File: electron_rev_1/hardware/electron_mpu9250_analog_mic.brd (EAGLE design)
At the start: 22.2 x 102.8 mm, 43 parts, among them IC2 S25FL128SAGNFI011, IC4 MIC_I2S_SPH0645, U1 MPU-9250, U10 GAS_SENSOR, U2 Value, U3 OPA322AIDBVT, U4 microSD, U5 +12v, U6 +12v, U7 GAS_SENSOR

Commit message: mainly cosmetic changes to schematic. changed label types
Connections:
- removed net AUX_CL: U1.7
- removed net AUX_DA: U1.21
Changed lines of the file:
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@@
 <contactref element="U7" pad="HB"/>
 <contactref element="U10" pad="HB"/>
-<contactref element="U4" pad="CD2"/>
 <contactref element="U4" pad="6"/>
 <contactref element="U4" pad="GND1"/>
@@
 <via x="18.81" y="-6.02" extent="1-16" drill="0.2"/>
 <via x="5.36" y="13.64" extent="1-16" drill="0.2"/>
+<contactref element="U4" pad="CD2"/>
 </signal>
 <signal name="TX">
@@
 <wire x1="10.36" y1="23.95" x2="10.08" y2="23.67" width="0.2032" layer="1"/>
 </signal>
-<signal name="AUX_CL">
-<contactref element="U1" pad="7"/>
-</signal>
-<signal name="AUX_DA">
-<contactref element="U1" pad="21"/>
-</signal>
 <signal name="N$1">

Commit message: ugh. stupid error in solder jumpers
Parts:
- moved SJ1 0.28 mm to (2.59, -18.4)
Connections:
- new net N$10: SJ1.1, SJ2.2, U5.1
- net VBAT: no longer SJ1.1, SJ2.2, U5.1
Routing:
- net VBAT: track 45.6 -> 24.9 mm, vias 2 -> 1
- net N$10: track 0.00 -> 20.0 mm, vias 0 -> 1
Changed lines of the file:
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@@
 </element>
 <element name="L1" library="logos" package="UCB_CAL_100MIL" value="UCB_CAL100MIL" x="13.66" y="24.52"/>
-<element name="SJ1" library="jumper" library_urn="urn:adsk.eagle:library:252" package="SJ" package3d_urn="urn:adsk.eagle:package:15471/1" value="" x="2.87" y="-18.37" smashed="yes" rot="R90">
-<attribute name="VALUE" x="2.87" y="-17.9699" size="0.02" layer="27" rot="R90"/>
+<element name="SJ1" library="jumper" library_urn="urn:adsk.eagle:library:252" package="SJ" package3d_urn="urn:adsk.eagle:package:15471/1" value="" x="2.59" y="-18.42" smashed="yes" rot="R90">
+<attribute name="VALUE" x="2.59" y="-18.0199" size="0.02" layer="27" rot="R90"/>
 </element>
 <element name="SJ2" library="jumper" library_urn="urn:adsk.eagle:library:252" package="SJ" package3d_urn="urn:adsk.eagle:package:15471/1" value="" x="3.31" y="-37.78" smashed="yes" rot="R180">
@@
 <wire x1="2.8227" y1="4.5713125" x2="2.8227" y2="0.9686875" width="0.508" layer="16"/>
 <wire x1="2.8227" y1="0.9686875" x2="2.85" y2="0.8359875" width="0.508" layer="16"/>
-<wire x1="2.85" y1="0.8359875" x2="2.85" y2="-15.34" width="0.508" layer="16"/>
-<wire x1="2.85" y1="-15.34" x2="2.86" y2="-15.35" width="0.508" layer="16"/>
-<via x="2.85" y="-15.34" extent="1-16" drill="0.35"/>
-<wire x1="2.87" y1="-15.36" x2="2.85" y2="-15.34" width="0.508" layer="1"/>
+<wire x1="2.85" y1="0.8359875" x2="2.82" y2="-15.33" width="0.508" layer="16"/>
+<wire x1="2.82" y1="-15.33" x2="2.86" y2="-15.35" width="0.508" layer="16"/>
+<via x="2.82" y="-15.33" extent="1-16" drill="0.35"/>
+<wire x1="2.87" y1="-15.36" x2="2.82" y2="-15.33" width="0.508" layer="1"/>
 <contactref element="SJ1" pad="2"/>
-<wire x1="2.85" y1="-15.34" x2="2.85" y2="-17.108" width="0.508" layer="1"/>
-<wire x1="2.85" y1="-17.108" x2="2.87" y2="-17.608" width="0.508" layer="1"/>
-<contactref element="SJ2" pad="2"/>
-<contactref element="U5" pad="1"/>
-<contactref element="SJ1" pad="1"/>
-<wire x1="1.26" y1="-31.22" x2="2.51" y2="-31.22" width="0.508" layer="16"/>
-<wire x1="2.51" y1="-31.22" x2="2.54" y2="-31.25" width="0.508" layer="16"/>
-<wire x1="2.54" y1="-31.25" x2="2.6" y2="-31.25" width="0.508" layer="16"/>
-<wire x1="2.6" y1="-31.25" x2="2.68" y2="-31.17" width="0.508" layer="16"/>
-<via x="2.68" y="-31.17" extent="1-16" drill="0.35"/>
-<wire x1="2.68" y1="-31.17" x2="2.64" y2="-18.8472" width="0.508" layer="1"/>
-<wire x1="2.87" y1="-19.132" x2="2.87" y2="-19.0772" width="0.4064" layer="1"/>
-<wire x1="2.87" y1="-19.0772" x2="2.64" y2="-18.8472" width="0.4064" layer="1"/>
-<wire x1="2.548" y1="-37.78" x2="2.618" y2="-31.232" width="0.4064" layer="1"/>
-<wire x1="2.618" y1="-31.232" x2="2.68" y2="-31.17" width="0.4064" layer="1"/>
-<wire x1="2.87" y1="-17.608" x2="2.64" y2="-18.8472" width="0" layer="19" extent="1-1"/>
+<wire x1="2.82" y1="-15.33" x2="2.85" y2="-17.108" width="0.508" layer="1"/>
+<wire x1="2.85" y1="-17.108" x2="2.59" y2="-17.658" width="0.508" layer="1"/>
 </signal>
 <signal name="D7">
@@
 <via x="17.44" y="-31.23" extent="1-16" drill="0.35"/>
 <wire x1="17.44" y1="-31.23" x2="17.42" y2="-31.21" width="0.4064" layer="1"/>
-<wire x1="4.072" y1="-37.78" x2="4.072" y2="-36.278" width="0.4064" layer="1"/>
-<wire x1="4.072" y1="-36.278" x2="9.1" y2="-31.25" width="0.4064" layer="1"/>
+<wire x1="4.072" y1="-37.78" x2="4.082" y2="-36.538" width="0.4064" layer="1"/>
+<wire x1="4.082" y1="-36.538" x2="9.1" y2="-31.25" width="0.4064" layer="1"/>
 <wire x1="9.1" y1="-31.25" x2="17.42" y2="-31.25" width="0.4064" layer="1"/>
 <wire x1="17.42" y1="-31.25" x2="17.44" y2="-31.23" width="0.4064" layer="1"/>
 </signal>
+<signal name="N$10">
+<contactref element="SJ2" pad="2"/>
+<contactref element="SJ1" pad="1"/>
+<contactref element="U5" pad="1"/>
+<wire x1="1.26" y1="-31.22" x2="2.58" y2="-31.24" width="0.4064" layer="16"/>
+<wire x1="2.58" y1="-31.24" x2="2.57" y2="-31.17" width="0.4064" layer="16"/>
+<via x="2.57" y="-31.17" extent="1-16" drill="0.35"/>
+<wire x1="2.57" y1="-31.17" x2="2.548" y2="-37.78" width="0.4064" layer="1"/>
+<wire x1="2.59" y1="-19.182" x2="2.57" y2="-31.17" width="0.4064" layer="1"/>
+</signal>
 </signals>

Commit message: cosmetic changes
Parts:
- C2, C8: value (none) -> 2.2uF
- C4: value (none) -> 16pF
- C7: value (none) -> 25uF
- R12, R8, R9: value (none) -> 100K
- R13: value (none) -> 49.9
- R14: value (none) -> 75K
- R15, R7: value 68 -> (none)
- R6: value (none) -> 13.7K
- U5, U6: value +12v -> +5v
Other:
- board text added: "A lines ok?"
- board text added: "MIC footprint..."
- board text added: "VCC lines ok by mem?"
- board text added: "overlapping SPI lines?"

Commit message: before ripping everything up and removing the timer
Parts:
- removed IC2: S25FL128SAGNFI011, S25FL128SAGNFI011:SON127P800X600X80-9N
- removed R3: 54.9K, resistor:R0603
- removed R4: 196K, resistor:R0603
- removed SJ1, SJ2: (no value), jumper:SJ
- removed U2: Value, TPL5010:DDC0006A_N
- removed U6: +5v, SparkFun-IC-Power:TO-252
- removed U7: GAS_SENSOR, SparkFun:MQ-3
- added C10: 2.2uF, SparkFun-Capacitors:0603-CAP
- added C11: 220uF, SparkFun-Capacitors:0603-CAP
- added C12: 10uF, SparkFun-Capacitors:0603-CAP
- added C9: 4.7uF, SparkFun-Capacitors:0603-CAP
- added L2: 6.8uH, resistor:L3225P
- added R18, R19, R20: 10K, resistor:R0603
- added R21, R22, R23, R24: (no value), resistor:R0603
- R17: value 10k -> (none)
- U5: value +5v -> TPS61030PWPR; device SparkFun-IC-Power:TO-252 -> TPS61030PWPR:PWP16_2P31X2P46
- moved R16 20.3 mm to (5.17, -34.0), turned to 0 degrees
- moved L1 19.1 mm to (14.5, 43.6)
- moved R17 13.4 mm to (6.83, -42.9), turned to 180 degrees
- moved U5 8.23 mm to (11.4, -38.3), flipped to the top, turned to 0 degrees
- moved C3 2.97 mm to (16.0, 26.6), turned to 0 degrees
- moved U10 0.12 mm to (10.8, -25.4), turned to 180 degrees
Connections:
- removed net D6: U$5.6
- removed net H2: U6.2, U7.A1, U7.HA
- new net C_DET: R18.1, U$5.6, U4.CD1
- new net EN: U5.9
- new net LBO: R24.1, U5.10
- new net N$12: R17.2, R21.1, U5.7
- net A1: no longer U2.6
- net B1: now also R16.2, U10.B1
- net B2: no longer R16.2, U10.B1
- net B3: no longer R17.2, U7.B1
- net DAC: no longer U2.5
- net GND: now also C10.2, C11.2, C12.2, C9.2, R23.1, U5.11, U5.4, U5.5, U5.8; no longer IC2.4, R3.1, R4.1, U2.2, U6.3, U7.HB
- net H1: now also C10.1, C11.1, R22.2, R24.2, U5.13, U5.14, U5.15; no longer U5.2
- net MISO: no longer IC2.2
- net MOSI: now also R20.1; no longer IC2.5
- net N$10: now also L2.2, U5.2; no longer SJ1.1, SJ2.2
- net N$11: now also R22.1, R23.2, U5.12; no longer SJ2.1, U6.1
- net SCK: no longer IC2.6
- net SS: now also R19.1; no longer IC2.1
- net VBAT: now also C12.1, L2.1, R21.2, U5.6; no longer SJ1.2
- net VCC: now also C9.1, R18.2, R19.2, R20.2; no longer IC2.8, R3.2, R4.2, U2.1, U2.3
- net WKP: no longer U2.4
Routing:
- net B3: track 84.7 -> 1.63 mm
- net B2: track 70.8 -> 0.00 mm
- net MISO: track 56.6 -> 0.00 mm, vias 2 -> 0
- net C_DET: track 0.00 -> 47.4 mm, vias 0 -> 1
- net VBAT: track 24.8 -> 55.4 mm
- net BCLK: track 25.5 -> 0.00 mm, vias 1 -> 0
- net H2: track 25.2 -> 0.00 mm, vias 1 -> 0
- net H1: track 9.69 -> 29.7 mm, vias 0 -> 2
- net A1: track 17.5 -> 0.00 mm, vias 3 -> 0
- net SS: track 58.3 -> 41.3 mm, vias 2 -> 1
- net N$11: track 19.1 -> 4.47 mm, vias 1 -> 0
- net N$10: track 20.0 -> 6.04 mm, vias 1 -> 0
- net VCC: track 116.4 -> 125.6 mm, vias 7 -> 5
- net B1: track 0.00 -> 5.75 mm
- net N$12: track 0.00 -> 5.19 mm
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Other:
- board size 22.2 x 102.8 mm -> 23.2 x 93.8 mm
- board text added: "boost regulator"
- board text added: "turn off gas sensors"
- board text removed: "GAS0"
- board text removed: "GAS1"

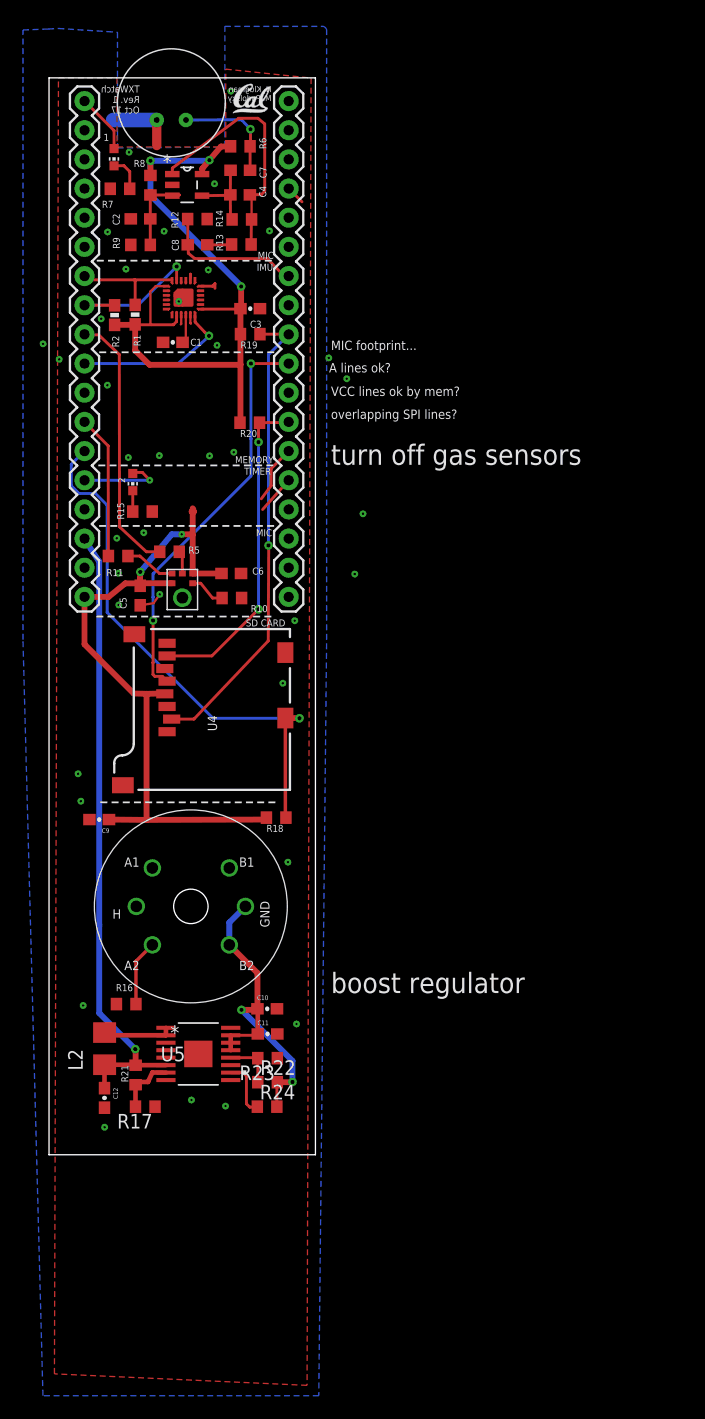
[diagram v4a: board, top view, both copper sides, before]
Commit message: reroute with a single gas sensor
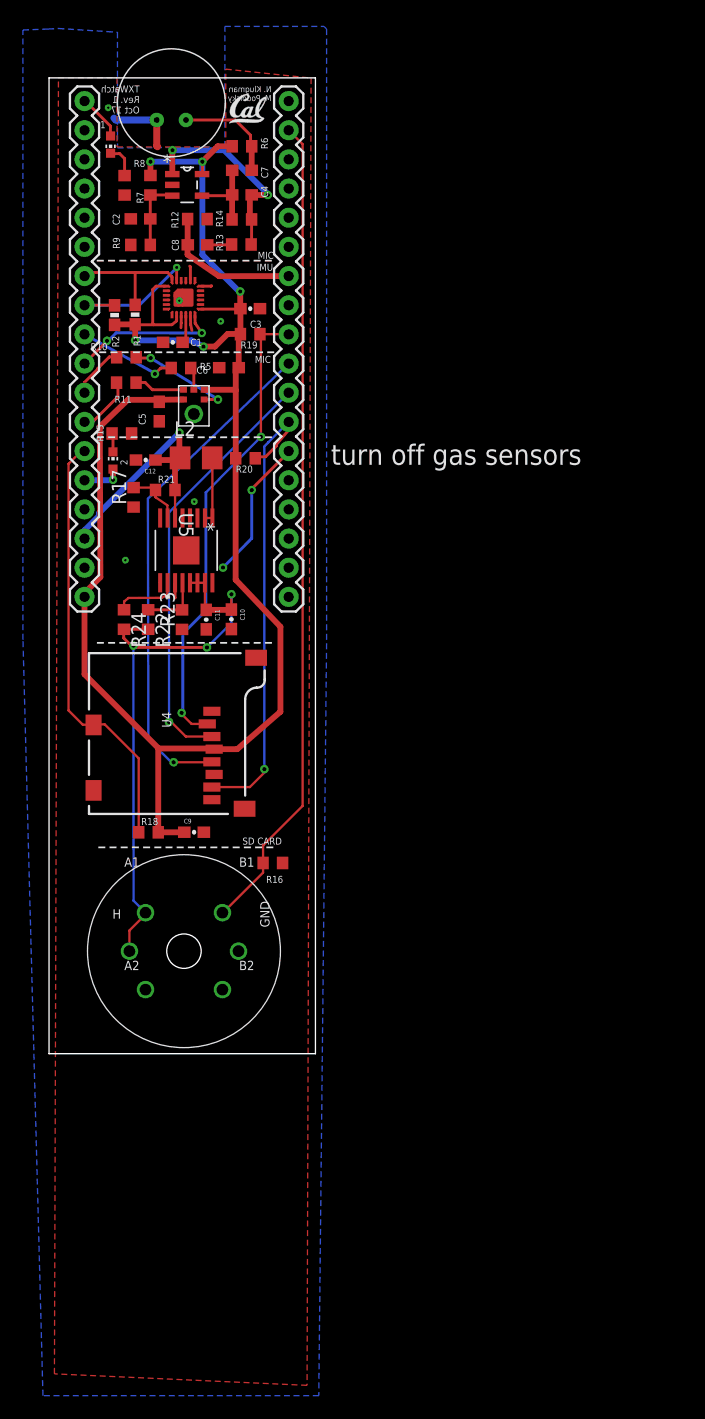
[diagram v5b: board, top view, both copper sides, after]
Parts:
- moved C12 55.7 mm to (6.87, 13.4), turned to 180 degrees
- moved R17 53.1 mm to (5.81, 10.2), turned to 90 degrees
- moved L2 52.1 mm to (11.3, 13.6), turned to 0 degrees
- moved R21 51.0 mm to (8.57, 10.8), turned to 0 degrees
- moved R24 44.2 mm to (4.98, -0.47), turned to 270 degrees
- moved U5 43.9 mm to (10.4, 5.55), turned to 270 degrees
- moved R22 41.6 mm to (7.08, -0.47), turned to 270 degrees
- moved R23 38.9 mm to (10.0, -0.48), turned to 90 degrees
- moved C11 36.5 mm to (12.1, -0.48), turned to 270 degrees
- moved C10 34.1 mm to (14.3, -0.45), turned to 270 degrees
- moved U4 23.8 mm to (1.93, -17.4), turned to 270 degrees
- moved R10 22.9 mm to (5.19, 22.4), turned to 180 degrees
- moved C6 17.9 mm to (14.1, 21.5), turned to 180 degrees
- moved R16 17.7 mm to (17.9, -21.7), turned to 180 degrees
- moved C5 16.1 mm to (8.05, 17.6)
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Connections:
- removed net DAC: U$4.13
- net EN: now also U$4.13
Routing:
- net B1: track 5.75 -> 71.9 mm
- net MISO: track 0.00 -> 37.3 mm, vias 0 -> 1
- net VBAT: track 55.4 -> 22.7 mm
- net VCC: track 125.6 -> 150.1 mm
- net H1: track 29.7 -> 53.1 mm, vias 2 -> 3
- net DATA: track 23.1 -> 8.67 mm, vias 0 -> 1
- net EN: track 0.00 -> 12.7 mm, vias 0 -> 2
- net MOSI: track 28.9 -> 41.6 mm, vias 2 -> 1
- net C_DET: track 47.4 -> 37.6 mm, vias 1 -> 0
- net SCK: track 35.4 -> 44.3 mm, vias 2 -> 1
- net WS: track 12.5 -> 5.14 mm
- net N$4: track 3.18 -> 9.38 mm, vias 0 -> 2
- net DAC: track 5.08 -> 0.00 mm
- net BCLK: track 0.00 -> 4.67 mm
- net D7: track 7.54 -> 3.44 mm
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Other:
- board size 23.2 x 93.8 mm -> 23.2 x 85 mm
- board text removed: "A lines ok?"
- board text removed: "MEMORY"
- board text removed: "MIC footprint..."
- board text removed: "TIMER"
- board text removed: "VCC lines ok by mem?"
- board text removed: "boost regulator"
- board text removed: "overlapping SPI lines?"

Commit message: ugh, rewire w out gas sensor. need to add fet for power cycling the sd card and then will ship
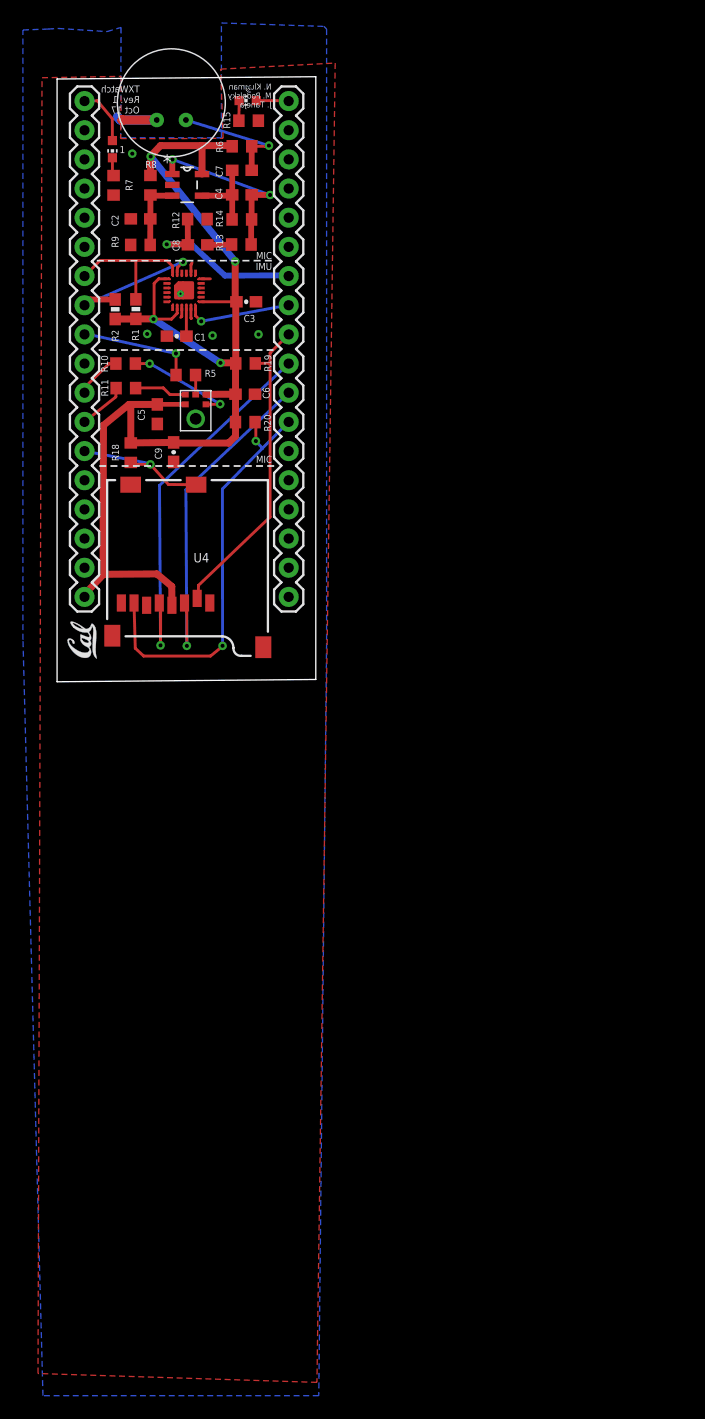
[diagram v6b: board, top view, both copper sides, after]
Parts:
- removed C10: 2.2uF, SparkFun-Capacitors:0603-CAP
- removed C11: 220uF, SparkFun-Capacitors:0603-CAP
- removed C12: 10uF, SparkFun-Capacitors:0603-CAP
- removed L2: 6.8uH, resistor:L3225P
- removed R16: 10k, resistor:R0603
- removed R17, R21, R22, R23, R24: (no value), resistor:R0603
- removed U10: GAS_SENSOR, SparkFun:MQ-3
- removed U5: TPS61030PWPR, TPS61030PWPR:PWP16_2P31X2P46
- moved L1 48.0 mm to (2.61, -3.86), turned to 90 degrees
- moved 2 33.5 mm to (15.8, 44.7), turned to 90 degrees
- moved C9 33.1 mm to (9.30, 14.1), turned to 270 degrees
- moved R18 33.1 mm to (5.57, 14.1), turned to 90 degrees
- moved R15 29.4 mm to (15.8, 43.0)
- moved U4 29.1 mm to (3.51, 11.7), turned to 180 degrees
- moved R20 3.15 mm to (15.5, 16.7)
- moved C6 2.71 mm to (15.5, 19.1), turned to 0 degrees
- moved R19 2.58 mm to (15.6, 21.8)
- moved R7 0.96 mm to (4.07, 37.3)
- moved R5 0.74 mm to (10.4, 20.8)
- moved C3 0.69 mm to (15.6, 27.2)
- moved U1 0.64 mm to (10.2, 28.2)
- moved C1 0.64 mm to (9.57, 24.2)
- moved R10 0.55 mm to (5.12, 21.8)
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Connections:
- removed net H1: C10.1, C11.1, R22.2, R24.2, U10.A1, U10.HA, U5.13, U5.14, U5.15
- removed net LBO: R24.1, U5.10
- removed net N$10: L2.2, U5.1, U5.2
- removed net N$11: R22.1, R23.2, U5.12
- removed net N$12: R17.2, R21.1, U5.7
- net A1: now also U1.12
- net B0: now also 2.A
- net B1: no longer R16.2, U10.B1
- net D3: no longer U1.12
- net D7: no longer 2.A
- net EN: no longer U5.9
- net GND: no longer C10.2, C11.2, C12.2, R16.1, R17.1, R23.1, U10.HB, U5.11, U5.3, U5.4, U5.5, U5.8
- net VBAT: no longer C12.1, L2.1, R21.2, U5.6
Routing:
- net B1: track 71.9 -> 0.00 mm
- net H1: track 53.1 -> 0.00 mm, vias 3 -> 0
- net VCC: track 150.1 -> 108.8 mm, vias 5 -> 4
- net C_DET: track 37.6 -> 12.5 mm, vias 0 -> 1
- net VBAT: track 22.7 -> 0.00 mm, vias 1 -> 0
- net SS: track 41.0 -> 27.7 mm, vias 2 -> 0
- net D3: track 13.0 -> 0.00 mm, vias 2 -> 0
- net EN: track 12.7 -> 0.00 mm, vias 2 -> 0
- net SCK: track 44.3 -> 33.1 mm
- net A1: track 0.00 -> 9.10 mm, vias 0 -> 1
- net MISO: track 37.3 -> 29.7 mm
- net N$10: track 6.06 -> 0.00 mm
- net LBO: track 5.71 -> 0.00 mm
- net N$11: track 5.51 -> 0.00 mm
- net N$12: track 5.25 -> 0.00 mm
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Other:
- board size 23.2 x 85 mm -> 22.5 x 52.7 mm
- board text added: "N. Klugman M. Podolsky J. Taneja"
- board text removed: "A1"
- board text removed: "A2"
- board text removed: "B1"
- board text removed: "B2"
- board text removed: "GND"
- board text removed: "H"
- board text removed: "N. Klugman M. Podolsky"
- board text removed: "SD CARD"
- board text removed: "turn off gas sensors"
